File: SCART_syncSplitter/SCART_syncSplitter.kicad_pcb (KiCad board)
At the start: 4 copper layers, 31 parts, among them J1 SCART-F, J2 VGA Out, J3 POWER IN, J4 HSync Selector, J5 Audio Out, U1 LMH1981, U2 L7805

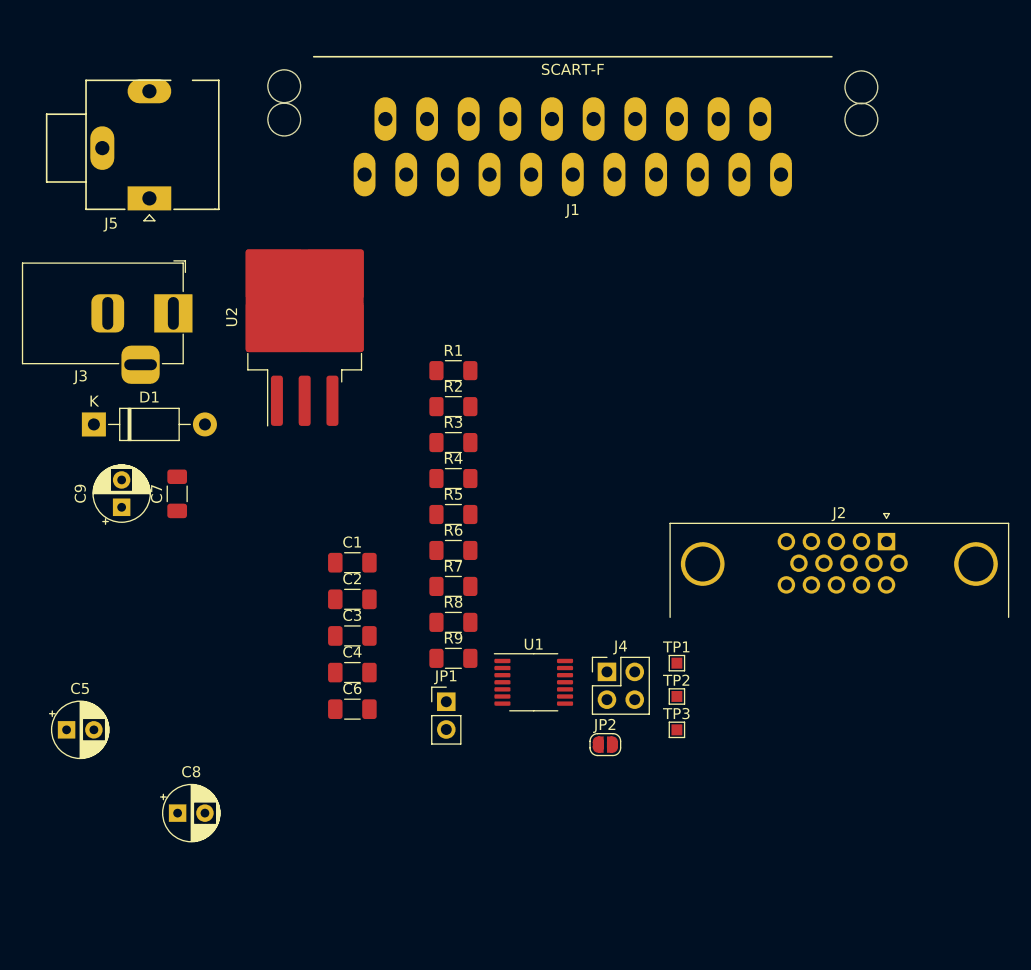
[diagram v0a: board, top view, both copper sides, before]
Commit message: Add Power led
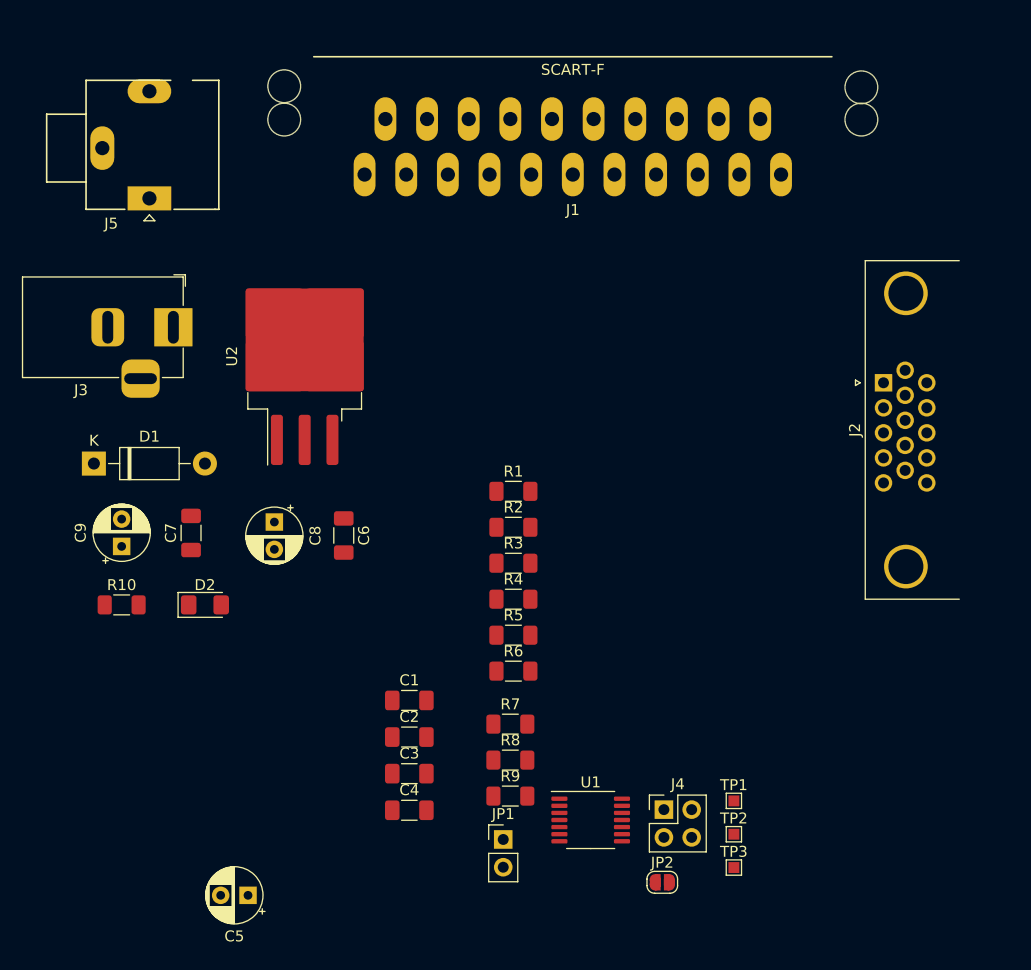
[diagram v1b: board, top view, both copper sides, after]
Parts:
- added D2: LED, LED_SMD:LED_1206_3216Metric_Pad1.42x1.75mm_HandSolder, F.Cu at (61.0, 69.8)
- added R10: 470, Resistor_SMD:R_1206_3216Metric_Pad1.30x1.75mm_HandSolder, F.Cu at (53.3, 69.8)
- moved C8 28.1 mm to (67.3, 62.3), turned to -90 degrees
- moved C5 22.5 mm to (64.9, 96.4), turned to 180 degrees
- moved C6 15.9 mm to (73.7, 63.5), turned to -90 degrees
- moved J2 14.5 mm to (123.0, 49.5), turned to 90 degrees
- moved R7 13.6 mm to (88.9, 80.8)
- moved R9 13.6 mm to (88.9, 87.3)
- moved C1 13.6 mm to (79.7, 78.6)
- moved C3 13.6 mm to (79.7, 85.3)
- moved JP1 13.6 mm to (88.2, 91.3)
- moved JP2 13.6 mm to (102.8, 95.2)
- moved J4 13.6 mm to (103.0, 88.6)
- moved R8 13.6 mm to (88.9, 84.0)
- moved C2 13.6 mm to (79.7, 81.9)
- moved C4 13.6 mm to (79.7, 88.6)
- moved TP1 13.6 mm to (109.3, 87.8)
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
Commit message: Update the PCB
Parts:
- moved J2 5.08 mm to (118.0, 49.5)
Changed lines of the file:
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@@
   )
   (footprint "Connector_Dsub:DSUB-15-HD_Female_Horizontal_P2.29x1.98mm_EdgePinOffset3.03mm_Housed_MountingHolesOffset4.94mm" (layer "F.Cu")
-    (at 123.04 49.53 90)
+    (at 117.96 49.53 90)
     (descr "15-pin D-Sub connector, horizontal/angled (90 deg), THT-mount, female, pitch 2.29x1.98mm, pin-PCB-offset 3.0300000000000002mm, distance of mounting holes 25mm, distance of mounting holes to PCB edge 4.9399999999999995mm, see https://disti-assets.s3.amazonaws.com/tonar/files/datasheets/16730.pdf")
     (tags "15-pin D-Sub connector horizontal angled 90deg THT female pitch 2.29x1.98mm pin-PCB-offset 3.0300000000000002mm mounting-holes-distance 25mm mounting-hole-offset 25mm")

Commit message: Begin routing traces
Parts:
- JP2, TP1, TP2, TP3: moved to B.Cu
- moved C5 69.5 mm to (108.0, 41.9), turned to -90 degrees
- moved C4 50.5 mm to (101.6, 43.2), turned to 90 degrees
- moved TP1 47.8 mm to (101.6, 40.6), turned to 180 degrees
- moved TP2 47.0 mm to (101.6, 44.5), turned to 180 degrees
- moved TP3 46.3 mm to (101.6, 48.3), turned to 180 degrees
- moved C2 45.8 mm to (88.9, 37.1), turned to -90 degrees
- moved C1 43.9 mm to (94.0, 37.1), turned to -90 degrees
- moved JP1 42.9 mm to (110.5, 54.6), turned to -90 degrees
- moved U1 42.8 mm to (91.8, 47.0)
- moved JP2 39.8 mm to (114.3, 57.1)
- moved C3 38.4 mm to (82.8, 47.0)
- moved R8 33.8 mm to (82.8, 50.8), turned to 180 degrees
- moved R9 33.3 mm to (82.8, 54.6), turned to 180 degrees
- moved D2 31.4 mm to (91.7, 63.5)
- moved R10 31.4 mm to (84.1, 63.5)
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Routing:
- net GND: track 0.00 -> 372.4 mm, vias 0 -> 15
- net /HSync_OUT: track 0.00 -> 39.5 mm
- net Net-(D1-K): track 0.00 -> 30.2 mm, vias 0 -> 2
- net Net-(J4-Pin_1): track 0.00 -> 20.0 mm
- net Net-(JP1-A): track 0.00 -> 19.6 mm
- net /COMPOSITE_IN: track 0.00 -> 16.4 mm
- net Net-(D1-A): track 0.00 -> 14.2 mm
- net /VSync_OUT: track 0.00 -> 10.4 mm
- net /CSync_OUT: track 0.00 -> 9.88 mm
- net Net-(JP2-B): track 0.00 -> 7.92 mm
- net VCC: vias 0 -> 1
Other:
- board outline added: 74.9 x 48.3 mm

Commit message: Drawn pcb
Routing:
- net VCC: track 0.00 -> 132.4 mm, vias 1 -> 2
- net /S_BLUE: track 0.00 -> 48.8 mm
- net GND: track 372.4 -> 330.2 mm, vias 15 -> 14
- net /S_GREEN: track 0.00 -> 39.6 mm
- net /AUDIO_L: track 0.00 -> 32.4 mm
- net /S_RED: track 0.00 -> 28.6 mm
- net /AUDIO_R: track 0.00 -> 24.4 mm
- net /FILT_COMPOSITE: track 0.00 -> 11.9 mm, vias 0 -> 2
- net Net-(C1-Pad1): track 0.00 -> 11.1 mm
- net Net-(U1-OE): track 0.00 -> 10.3 mm, vias 0 -> 1
- net Net-(U1-BP): track 0.00 -> 7.53 mm, vias 0 -> 1
- net Net-(U1-VF): track 0.00 -> 6.97 mm, vias 0 -> 1
- net Net-(U1-VSync): track 0.00 -> 6.20 mm
- net Net-(U1-HSync): track 0.00 -> 5.29 mm
- net Net-(U1-Rext): track 0.00 -> 5.27 mm
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- added copper zone on B.Cu, net GND
- added copper zone on F.Cu, net GND
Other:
- copper layers 4 -> 2

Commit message: Update PCB and schematic
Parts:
- C1: value 570pF / OPEN -> 570pF
- JP1: value Disable VSync -> Enable VSync
- R2: value 100 / SHORT -> 100
- R5, R7, R9: value 10k/OPEN -> OPEN
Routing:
- net Net-(U1-CSync): track 0.00 -> 19.1 mm, vias 0 -> 2
- net GND: track 330.2 -> 345.1 mm, vias 14 -> 15
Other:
- board text added: "CSync"
- board text added: "HSync"

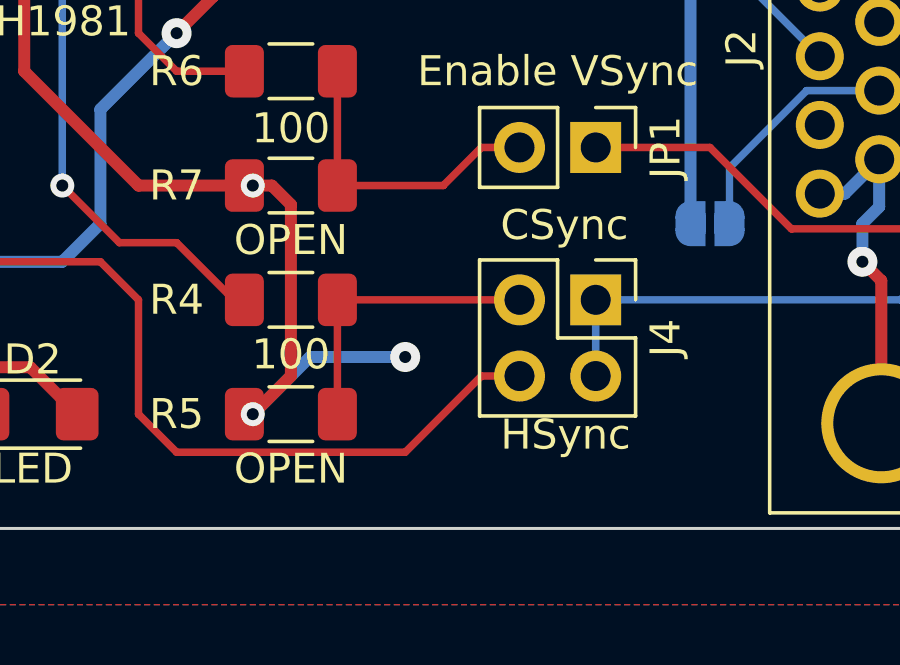
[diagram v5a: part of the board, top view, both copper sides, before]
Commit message: Added PCBWay logo
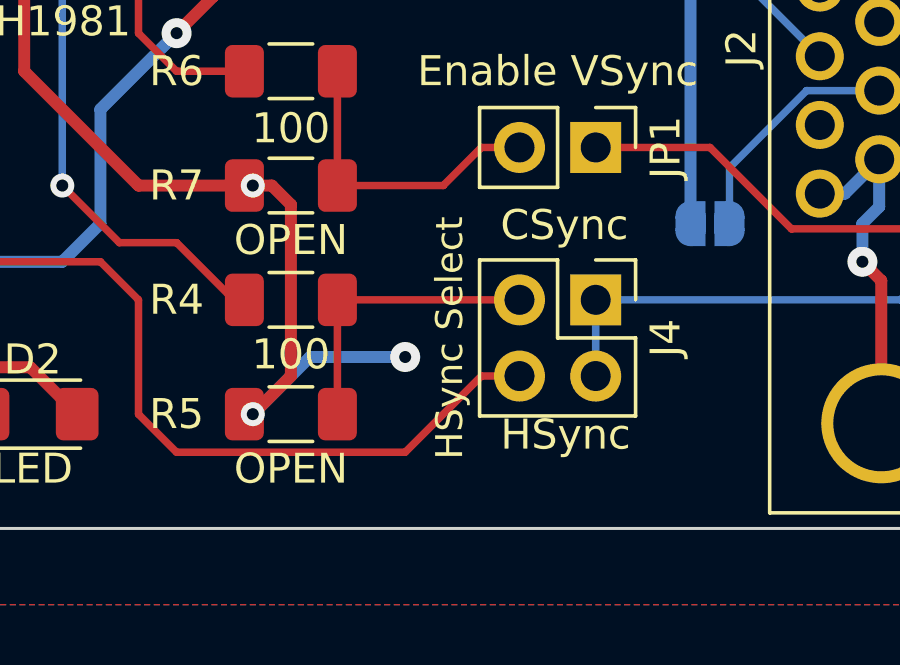
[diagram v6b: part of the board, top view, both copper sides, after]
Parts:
- added G***: LOGO, logos:PCBWay, B.Cu at (81.3, 53.3)
- J4: value HSync Selector -> HSync Select
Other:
- board text added: "Composite SYNC Splitter / Cleaner"
- board text added: "Rev. 0"
- board text added: "sponsored by"
